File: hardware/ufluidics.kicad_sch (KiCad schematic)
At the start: 0 parts

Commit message: Make the ESP32-S3 pin map work on N16R8 as well as N16
Octal PSRAM claims GPIO33-37 for the SPI0/1 data lines. The previous map put
STEP on 35-39, EN on 34 and a TMC UART on 33, so an R8 module would have
fought its own memory bus - building fine and then simply not pumping.

Moves STEP to GPIO38-42 (still contiguous, still in the GPIO_OUT1 bank, so the
single-register ISR write is unchanged) and relocates EN, both TMC UARTs, the
RUN switch, E-stop sense and I2C clear of 33-37. 26 pins used: 1 spare on R8,
6 on N16.

The SPI display header is the only thing left on 33-37 and is now compiled out
under BOARD_HAS_PSRAM, so R8 builds fall back to the I2C display.

A guarded static_assert catches any future pin that strays into the range.
Verified by deliberately moving EN_PIN to 34 and confirming the build fails,
then restoring it.

Both configurations build clean.
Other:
- added sheet mcu (mcu.kicad_sch)
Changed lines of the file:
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@@
 	(generator_version "10.0")
 	(paper "A4")
+	(sheet
+		(at 45.085 29.21)
+		(size 12.7 14.605)
+		(exclude_from_sim no)
+		(in_bom yes)
+		(on_board yes)
+		(dnp no)
+		(fields_autoplaced yes)
+		(stroke
+			(width 0.1524)
+			(type solid)
+		)
+		(fill
+			(color 0 0 0 0)
+		)
+		(property "Sheetname" "mcu"
+			(at 45.085 28.4984 0)
+			(show_name no)
+			(do_not_autoplace no)
+			(effects
+				(font
+					(size 1.27 1.27)
+				)
+				(justify left bottom)
+			)
+		)
+		(property "Sheetfile" "mcu.kicad_sch"
+			(at 45.085 44.3996 0)
+			(show_name no)
+			(do_not_autoplace no)
+			(effects
+				(font
+					(size 1.27 1.27)
+				)
+				(justify left top)
+			)
+		)
+		(instances
+			(project "ufluidics"
+				(path "/bf8ba2d7-3b7b-4865-bab6-5f38b618ecb0"
+					(page "2")
+				)
+			)
+		)
+	)
 	(sheet_instances
 		(path "/"

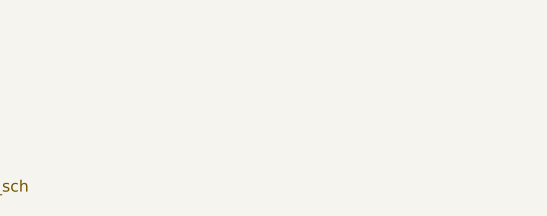
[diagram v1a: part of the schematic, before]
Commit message: Split the TMC2209 wiring by bare IC vs module
The driver table assumed a SilentStepStick, which hides the charge pump, sense
resistors and regulator capacitors on the module. A bare QFN-28 needs all of
them externally, and the pins involved are not optional: VS, VCP, CPI/CPO and
5VOUT drive the charge pump that generates high-side gate drive, and BRA/BRB
are the current sense returns.

Documents both cases, with the pin names that tell them apart, and notes the
real cost of bare ICs - about eight passives per driver, forty across the
board. Only DIAG, INDEX and NC are genuinely No-Connect either way.
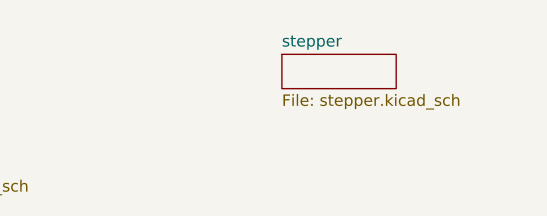
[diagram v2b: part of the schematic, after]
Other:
- added sheet stepper (stepper.kicad_sch)
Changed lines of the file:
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@@
+		)
+	)
+	(sheet
+		(at 90.17 30.48)
+		(size 12.7 3.81)
+		(exclude_from_sim no)
+		(in_bom yes)
+		(on_board yes)
+		(dnp no)
+		(fields_autoplaced yes)
+		(stroke
+			(width 0.1524)
+			(type solid)
+		)
+		(fill
+			(color 0 0 0 0)
+		)
+		(property "Sheetname" "stepper"
+			(at 90.17 29.7684 0)
+			(show_name no)
+			(do_not_autoplace no)
+			(effects
+				(font
+					(size 1.27 1.27)
+				)
+				(justify left bottom)
+			)
+		)
+		(property "Sheetfile" "stepper.kicad_sch"
+			(at 90.17 34.8746 0)
+			(show_name no)
+			(do_not_autoplace no)
+			(effects
+				(font
+					(size 1.27 1.27)
+				)
+				(justify left top)
+			)
+		)
+		(instances
+			(project "ufluidics"
+				(path "/bf8ba2d7-3b7b-4865-bab6-5f38b618ecb0"
+					(page "3")
+				)
+			)
 		)
 	)

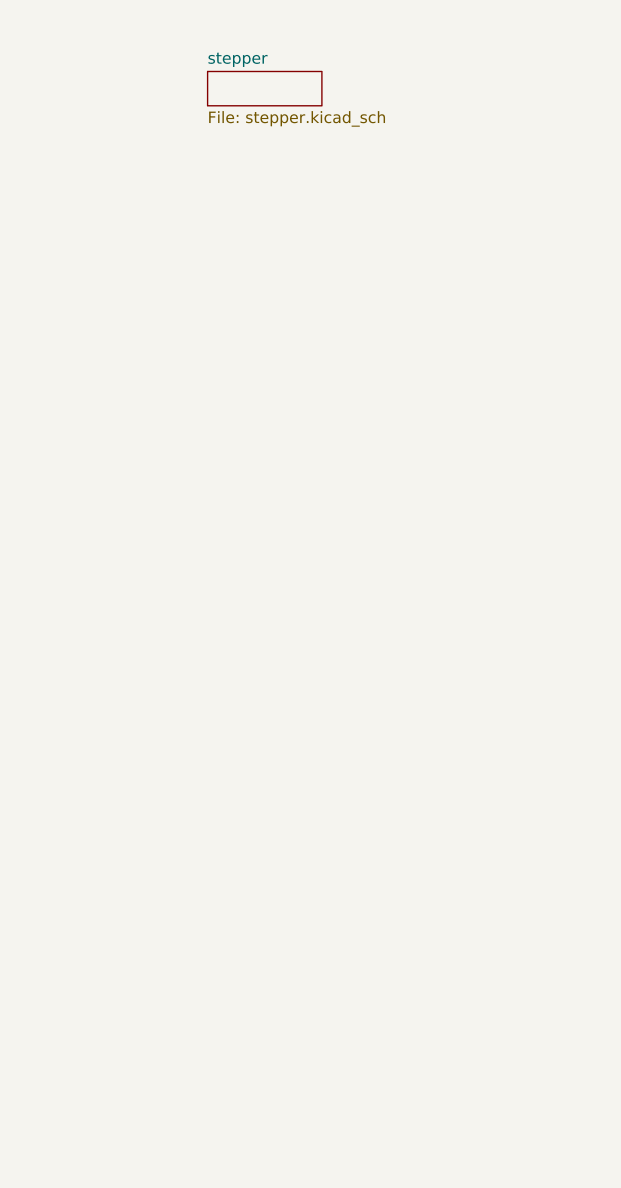
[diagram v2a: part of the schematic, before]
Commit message: Resolve the two-PDN-pad question for BigTreeTech modules
BTT TMC2209 V1.2/V1.3 breaks PDN_UART out on two alternative pin positions,
not as TX and RX. Pin 4 is the factory default with the 1k already fitted on
the module; pin 5 is physically open until that resistor is relocated.

So: wire pin 4 to the bus, leave pin 5 NC, and add no external resistor - a
second 1k in series would make 2k. Klipper drives these from a single uart_pin,
confirming single-wire half-duplex, so the pin budget is unchanged and both the
SPI display header and the R8 option survive.

Notes that this is vendor-specific: bare ICs and Watterott SilentStepSticks do
not carry the resistor, and some modules genuinely split TX/RX.

Source: https://global.bttwiki.com/TMC2209.html
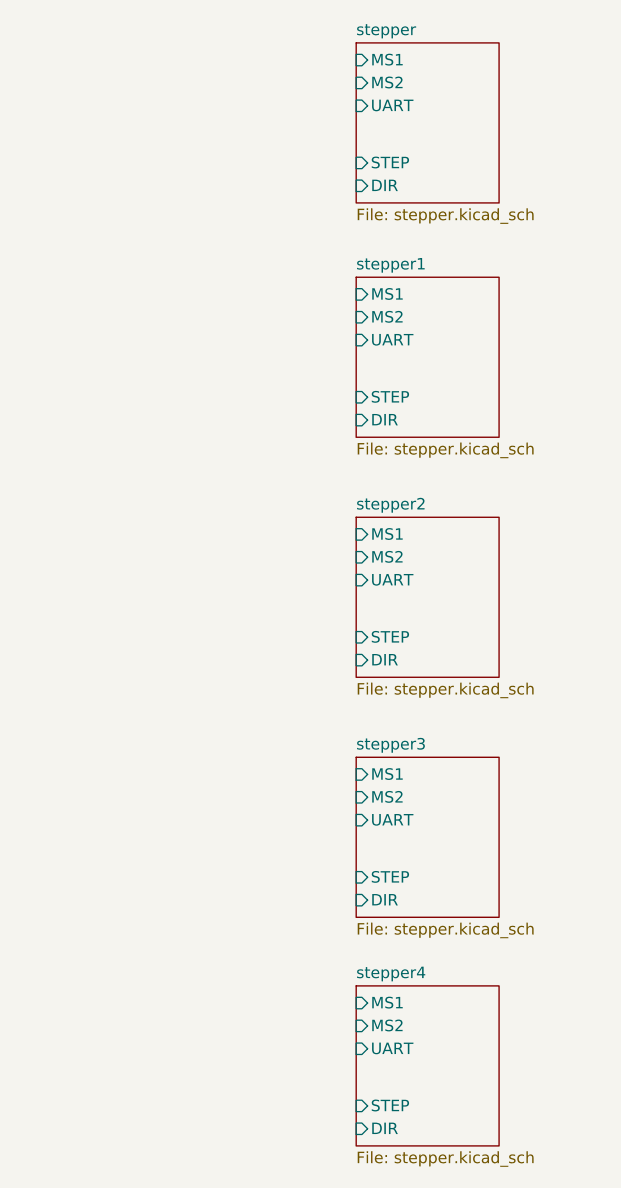
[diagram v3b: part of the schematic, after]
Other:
- added sheet stepper1 (stepper.kicad_sch)
- added sheet stepper2 (stepper.kicad_sch)
- added sheet stepper3 (stepper.kicad_sch)
- added sheet stepper4 (stepper.kicad_sch)
- sheet stepper ports: added DIR, MS1, MS2, STEP, UART; removed none

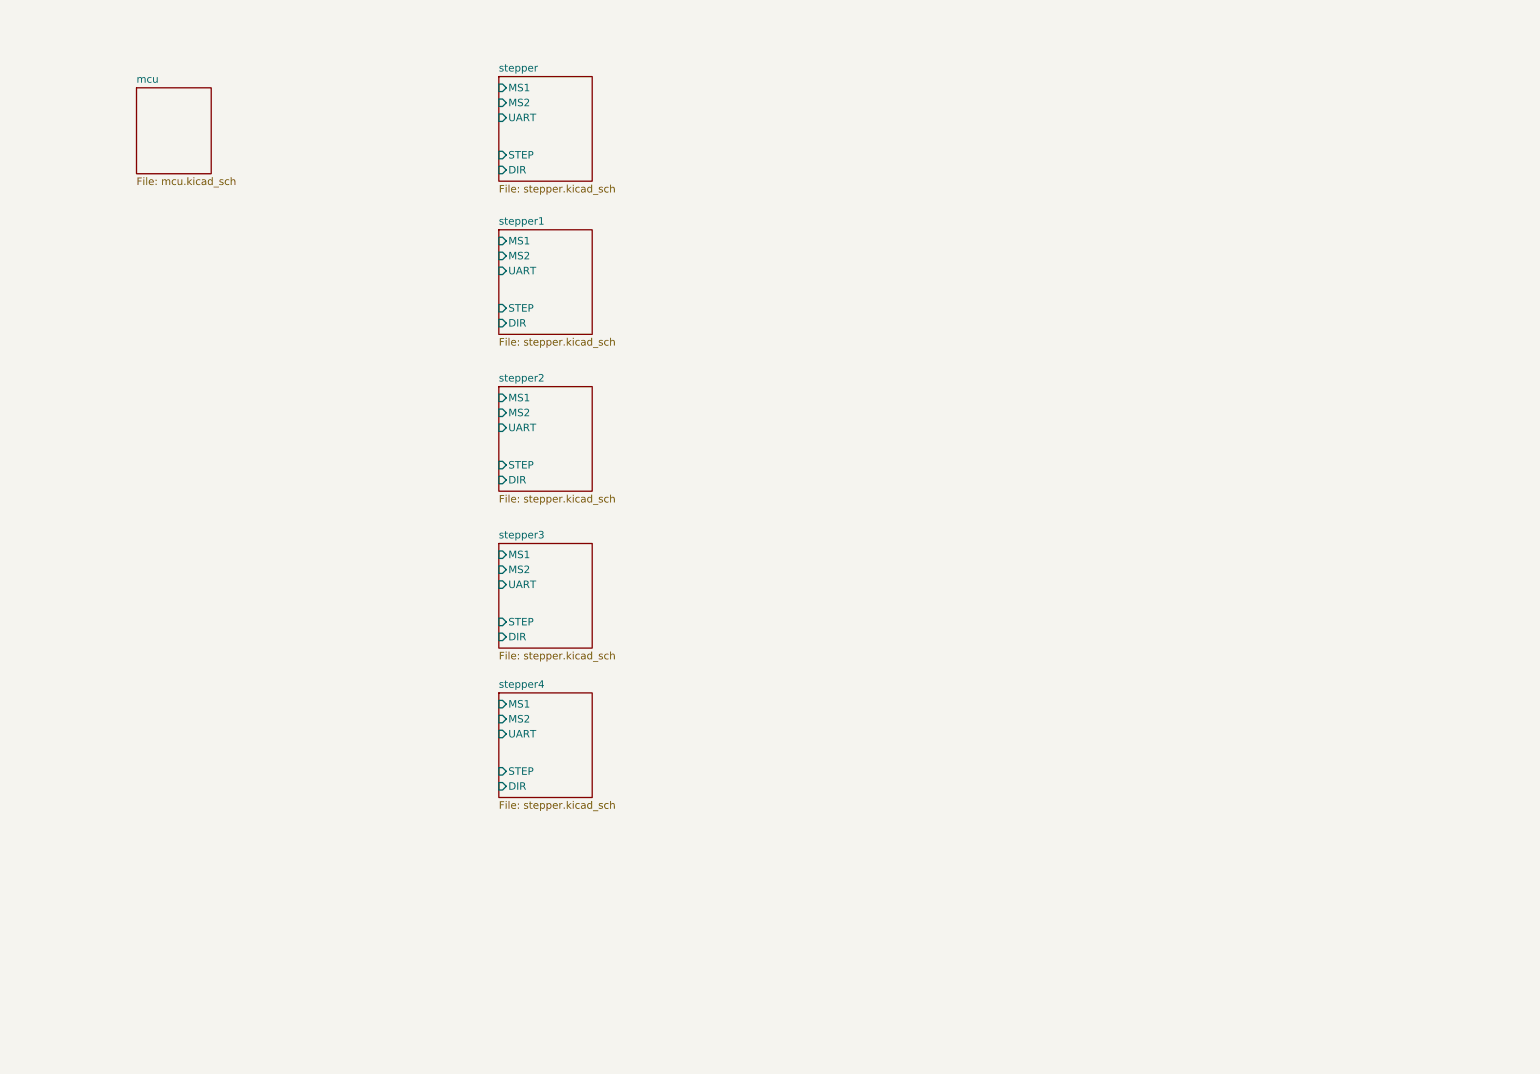
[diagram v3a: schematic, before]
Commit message: Switch to a low-dropout LDO; specify the VBUS Schottky
The 1117-family parts previously specified fail the USB-only case. From a
4.75 V VBUS minimum, a 0.35 V Schottky drop plus ~1 V of 1117 dropout leaves
3.40 V - only 100 mV of margin. A long cable, tired port or hub eats that, and
the symptom is an ESP32 resetting during Wi-Fi bursts, which presents as a
firmware bug.

AP7361C-33E-13: 140 mV dropout at 300 mA, 1 A, SOT-223, with current limit and
thermal shutdown. Same package and same 0.37 W, so the thermal analysis is
unchanged, and margin goes to ~960 mV.

Also specifies the VBUS Schottky. The binding spec is Vf at 250 mA read off the
curve, but the non-obvious one is reverse voltage: normal stress is ~5 V, yet a
shorted buck puts 24 V on the rail and this diode is the only thing between
that and the host USB port. SS34 at 40 V covers it.
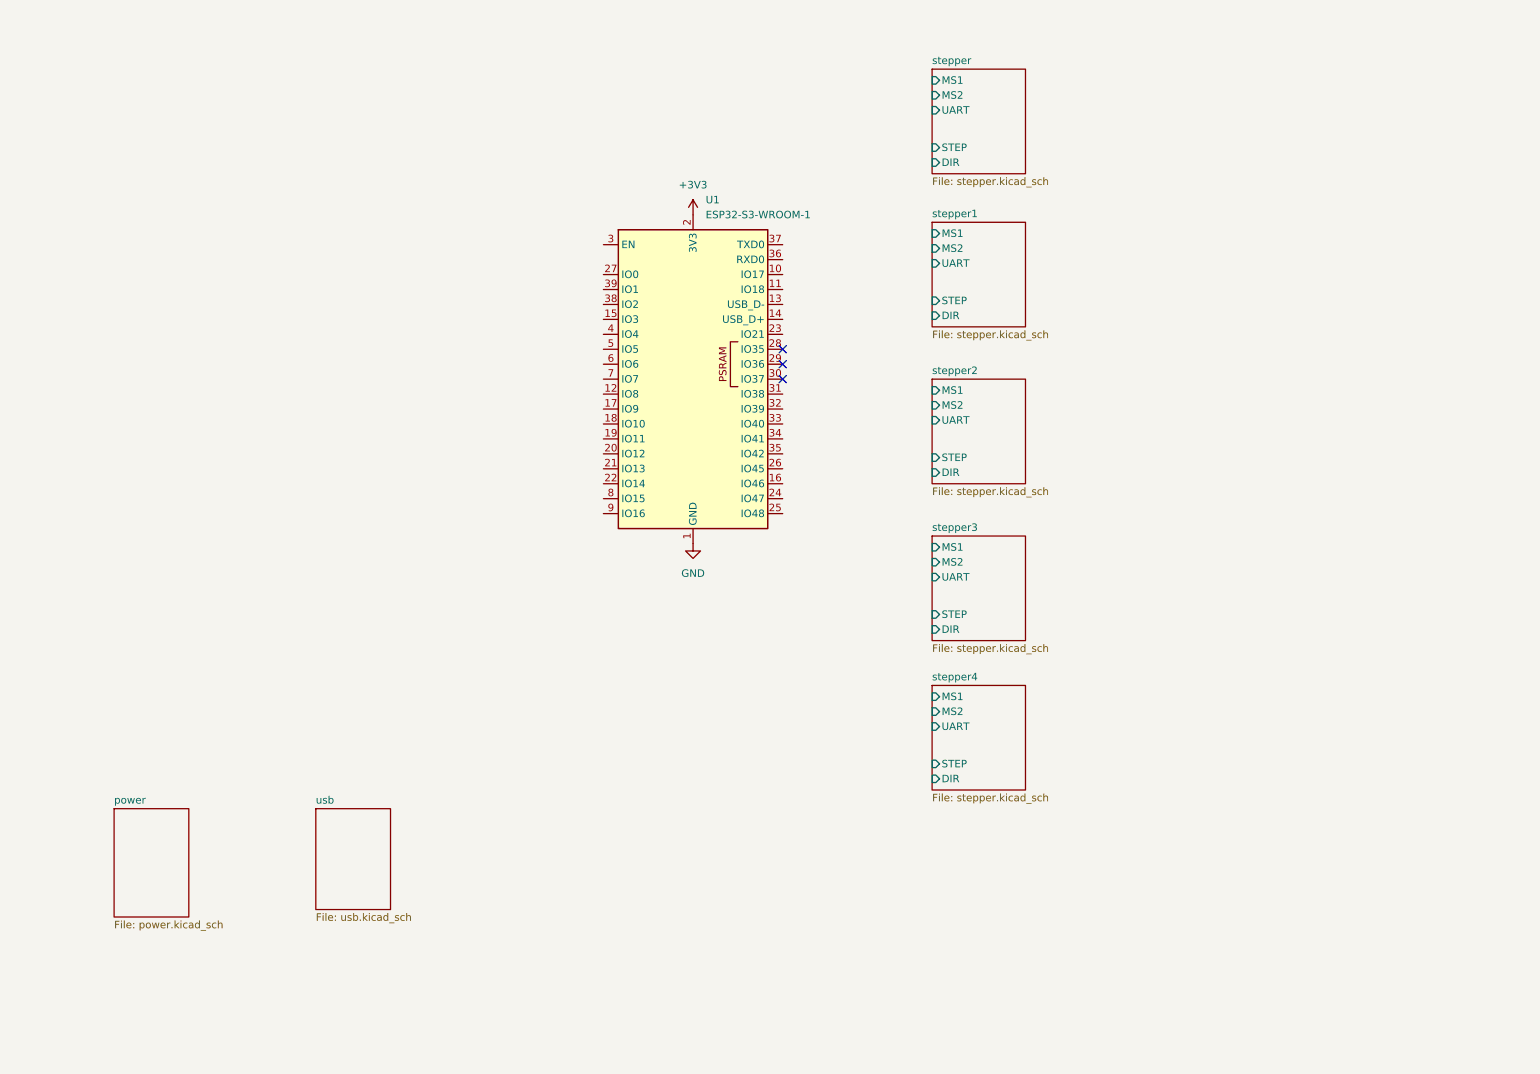
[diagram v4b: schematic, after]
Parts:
- added U1: ESP32-S3-WROOM-1, RF_Module:ESP32-S3-WROOM-1, symbol RF_Module:ESP32-S3-WROOM-1
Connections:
- new net +3V3: U1.2 (3V3)
- new net GND: U1.1 (GND), U1.40 (GND), U1.41 (GND)
- no-connect marks 0 -> 3
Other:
- removed sheet mcu
- added sheet power (power.kicad_sch)
- added sheet usb (usb.kicad_sch)

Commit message: make the schematics
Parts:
- added C2: 1uF, symbol Device:C
- added C3, C7: 100nF, symbol Device:C
- added C6: 22uF, symbol Device:C
- added J19: Conn_01x04, symbol Connector_Generic:Conn_01x04
- added J20: Conn_01x09, symbol Connector_Generic:Conn_01x09
- added J_ENDSTOP_OUT4: Conn_01x02, symbol Connector_Generic:Conn_01x02
- added R10, R9: 4.7k, symbol Device:R
- added R2, R3, R7: 10k, symbol Device:R
- added SW_BOOT1, SW_RST1: SW_Omron_B3FS, symbol Switch:SW_Omron_B3FS
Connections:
- net +3V3: now also C6.1, C7.1, J19.1 (Pin_1), J20.1 (Pin_1), J20.8 (Pin_8), R10.1, R2.1, R3.1, R7.1, R9.1
- net GND: now also C2.2, C3.2, C6.2, C7.2, J19.2 (Pin_2), J20.2 (Pin_2), J_ENDSTOP_OUT4.2 (Pin_2), SW_BOOT1.1, SW_RST1.1
- net TMC_UART_A: now reaches U1.10 (IO17)
- net TMC_UART_B: now reaches U1.11 (IO18)
- net IN1_ENDSTOP: now reaches U1.12 (IO8)
- net USB_DN: now reaches U1.13 (USB_D-)
- net USB_DP: now reaches U1.14 (USB_D+)
- net LED_FAULT: now reaches U1.16 (IO46)
- net IN2_ENDSTOP: now reaches U1.17 (IO9)
- net OUT1_ENDSTOP: now reaches U1.18 (IO10)
- net OUT2_ENDSTOP: now reaches U1.19 (IO11)
- net OUT3_ENDSTOP: now reaches U1.20 (IO12)
- net RUN_SWITCH: now reaches U1.21 (IO13)
- net RUN_SWITCH: now also J_ENDSTOP_OUT4.1 (Pin_1)
- net I2C_SCL: now reaches U1.23 (IO21)
- net I2C_SCL: now also J19.4 (Pin_4), R9.2
- net I2C_SDA: now reaches U1.24 (IO47)
- net I2C_SDA: now also J19.3 (Pin_3), R10.2
- net TFT_DC: now reaches U1.25 (IO48)
- net TFT_DC: now also J20.5 (Pin_5)
- net LED_RUN: now reaches U1.26 (IO45)
- net BOOT: now reaches U1.27 (IO0)
- net BOOT: now also R3.2, SW_BOOT1.2
- net TFT_SCK: now reaches U1.28 (IO35)
- net TFT_SCK: now also J20.7 (Pin_7)
- net TFT_MOSI: now reaches U1.29 (IO36)
- net TFT_MOSI: now also J20.6 (Pin_6)
- net EN/~RST: now reaches U1.3 (EN)
- net EN/~RST: now also C2.1, R2.2, SW_RST1.2
- net TFT_CS: now reaches U1.30 (IO37)
- net TFT_CS: now also J20.3 (Pin_3)
- net IN1_STEP: now reaches U1.31 (IO38)
- net IN2_STEP: now reaches U1.32 (IO39)
- net OUT1_STEP: now reaches U1.33 (IO40)
- net OUT2_STEP: now reaches U1.34 (IO41)
- net OUT3_STEP: now reaches U1.35 (IO42)
- net POT_B: now reaches U1.38 (IO2)
- net POT_A: now reaches U1.39 (IO1)
- net IN1_DIR: now reaches U1.4 (IO4)
- net IN2_DIR: now reaches U1.5 (IO5)
- net OUT1_DIR: now reaches U1.6 (IO6)
- net OUT2_DIR: now reaches U1.7 (IO7)
- net OUT3_DIR: now reaches U1.8 (IO15)
- net DRIVER_EN: now reaches U1.9 (IO16)
- new net TFT_RST: C3.1, J20.4 (Pin_4), R7.2
- no-connect marks 3 -> 5
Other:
- sheet stepper renamed stepper_IN1
- sheet stepper1 renamed stepper_IN2
- sheet stepper2 renamed stepper_OUT1
- sheet stepper3 renamed stepper_OUT2
- sheet stepper4 renamed stepper_OUT3
- added sheet endstops (endstops.kicad_sch)
- added sheet leds (leds.kicad_sch)
- added sheet pots (pots.kicad_sch)
- sheet usb ports: added USB_D+, USB_D-; removed none
- note added: "AKA SDI"
- note added: "BLK"
- note added: "BOOT switch"
- note added: "Decoupling capacitors"
- note added: "I2C Display"
- note added: "RESET switch"
- note added: "Stepper Drivers MS pins determine UART address, not microstepping"
- note added: "Switch, enables and disables stepper drivers. Does not cut power to MCU"
- note added: "TFT Display (ILI9341)"
- moved on the sheet: U1

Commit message: place the stuff on the pcb
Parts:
- removed C2: 1uF, symbol Device:C
- removed C3, C7: 100nF, symbol Device:C
- removed C6: 22uF, symbol Device:C
- removed R10, R9: 4.7k, symbol Device:R
- removed R2, R3, R7: 10k, symbol Device:R
- removed SW_BOOT1, SW_RST1: SW_Omron_B3FS, symbol Switch:SW_Omron_B3FS
- added C3: 22uF, PCM_JLCPCB:C_0805, symbol PCM_JLCPCB-Capacitors:0805,22uF
- added C6: 1uF, PCM_JLCPCB:C_0805, symbol PCM_JLCPCB-Capacitors:0805,1uF
- added Cinx1, Cinx2: 100nF, PCM_JLCPCB:C_0402, symbol PCM_JLCPCB-Capacitors:0402,100nF,(2)
- added J_DEBUG_UART1: Conn_01x03, Connector_JST:JST_XH_B3B-XH-A_1x03_P2.50mm_Vertical, symbol Connector_Generic:Conn_01x03
- added R1, R2, R3, R7: 10kΩ, PCM_JLCPCB:R_0603, symbol PCM_JLCPCB-Resistors:0603,10kΩ
- added R8, R9: 4.7kΩ, PCM_JLCPCB:R_0603, symbol PCM_JLCPCB-Resistors:0603,4.7kΩ
- added S1, S2: Tactile Button, 160gf, PCM_JLCPCB:SW_TS-1088-AR02016, symbol PCM_JLCPCB-Connectors_Buttons:Tactile Button, 160gf, 12V, 50mA, 4.0mm
- J19: footprint (none) -> Connector_JST:JST_XH_B4B-XH-A_1x04_P2.50mm_Vertical
- J20: footprint (none) -> Connector_JST:JST_XH_B9B-XH-A_1x09_P2.50mm_Vertical
- J_RUN_SWITCH1: renamed from J_ENDSTOP_OUT4; footprint (none) -> Connector_JST:JST_XH_B2B-XH-A_1x02_P2.50mm_Vertical
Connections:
- net +3V3: now also C3.1, Cinx2.1, R1.1, R2.1, R3.1, R7.1, R8.1, R9.1
- net BOOT: now also R2.2, S2.2 (B)
- net DRIVER_EN: now also R3.2
- net EN/~RST: now also C6.1, R1.2, S1.2 (B)
- net GND: now also C3.2, C6.2, Cinx1.2, Cinx2.2, J_DEBUG_UART1.3 (Pin_3), S1.1 (A), S2.1 (A)
- net I2C_SCL: now also R8.2
- net I2C_SDA: now also R9.2
- net TFT_RST: now also Cinx1.1, R7.2
- net DEBUG_RX: now reaches U1.36 (RXD0)
- net DEBUG_RX: now also J_DEBUG_UART1.1 (Pin_1)
- net DEBUG_TX: now reaches U1.37 (TXD0)
- net DEBUG_TX: now also J_DEBUG_UART1.2 (Pin_2)
- net USB_DN renamed USB_D_N
- net USB_DP renamed USB_D_P
- no-connect marks 5 -> 3
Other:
- note added: "Driver enable pull-up"
- note added: "UART Debug Connector"
